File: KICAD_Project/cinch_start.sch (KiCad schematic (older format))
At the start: 27 parts, among them P101 CONN_1, P102 CONN_1, P103 CONN_1, P104 CONN_1, P105 CONN_1, P109 CONN_1, P110 CONN_1, P111 CONN_1, P112 CONN_1, P113 CONN_1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

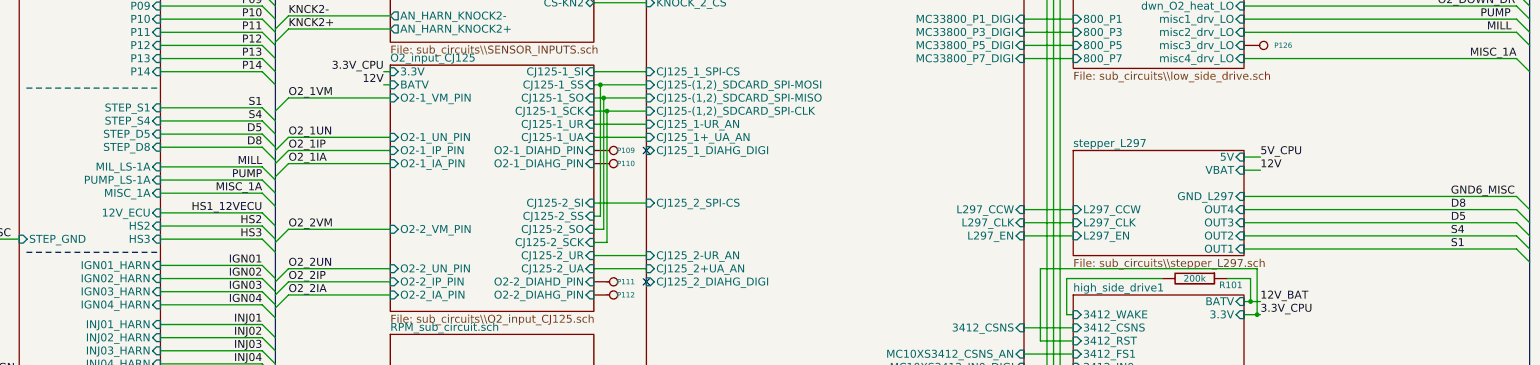
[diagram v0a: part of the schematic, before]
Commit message: changed stepper from L297 to A4988 from pololu
Signed-off-by: Jared Harvey <TortiseGIT@jaredharvey.com>
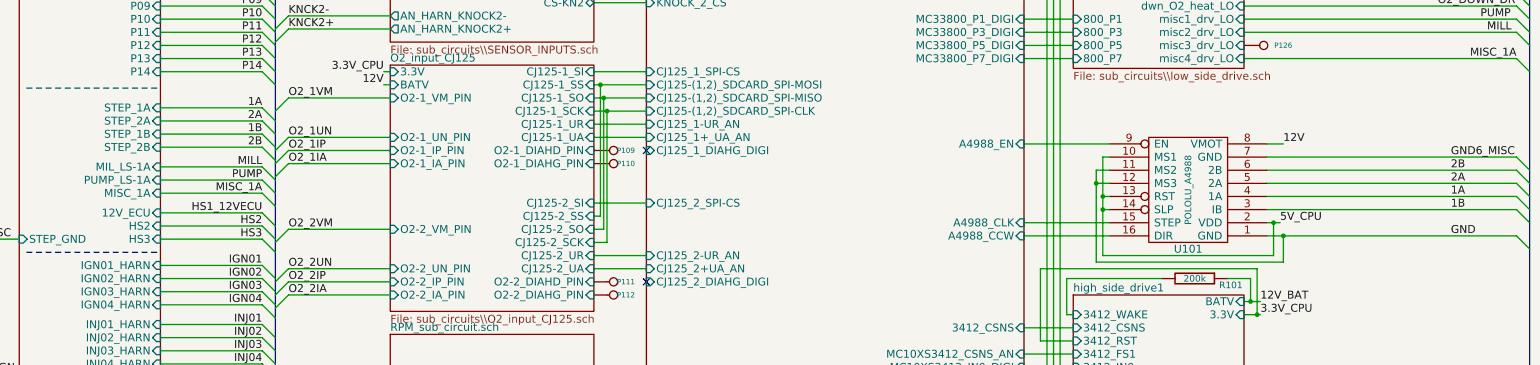
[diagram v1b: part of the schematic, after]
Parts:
- added U101: POLOLU_A4988, SWDIP8_.6W, symbol POLOLU_A4988
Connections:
- net 12V: now also U101.8 (VMOT)
- net 5V_CPU: now also U101.10 (MS1), U101.13 (RST), U101.14 (SLP), U101.2 (VDD)
- net GND: now also U101.1 (GND), U101.11 (MS2), U101.12 (MS3)
- net GND6_MISC: now also U101.7 (GND)
- new net 1A: U101.4 (1A)
- new net 1B: U101.3 (IB)
- new net 2A: U101.5 (2A)
- new net 2B: U101.6 (2B)
- new net CPU/A4988_CCW: U101.16 (DIR)
- new net CPU/A4988_CLK: U101.15 (STEP)
- new net CPU/A4988_EN: U101.9 (EN)
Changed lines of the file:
@@
-EESchema Schematic File Version 2  date 9/27/2011 11:45:21 AM
+EESchema Schematic File Version 2  date 10/2/2011 8:46:34 AM
 LIBS:power
 LIBS:device
@@
 $Descr C 22000 17000
 encoding utf-8
-Sheet 1 13
+Sheet 1 12
 Title "freeEMS PLUS from Cinch template "
-Date "27 sep 2011"
+Date "2 oct 2011"
 Rev "A-DRAFT5"
 Comp "diyefi.org/openecu.info"
@@
 Comment4 ""
 $EndDescr
+Connection ~ 13250 9525
+Connection ~ 14675 9925
+Wire Wire Line
+	14675 9925 14675 10125
+Wire Wire Line
+	14675 10125 13250 10125
+Wire Wire Line
+	13250 10125 13250 9425
+Wire Wire Line
+	16450 9325 14550 9325
+Wire Wire Line
+	12700 9925 13350 9925
+Wire Wire Line
+	12700 9225 13350 9225
+Connection ~ 13300 9625
+Wire Wire Line
+	13300 9625 13350 9625
+Wire Wire Line
+	16450 9925 14550 9925
+Connection ~ 14600 9825
+Wire Wire Line
+	14600 9825 14600 10075
+Wire Wire Line
+	14600 10075 13300 10075
+Wire Wire Line
+	13300 10075 13300 9325
 Wire Wire Line
 	12700 8575 13075 8575
@@
 Wire Wire Line
 	14375 8075 16450 8075
-Wire Wire Line
-	14375 9625 16450 9625
 Wire Wire Line
 	14375 5425 16450 5425
@@
 	14375 11525 16450 11525
 Wire Wire Line
-	14375 9925 16450 9925
-Wire Wire Line
-	14375 10025 16450 10025
-Wire Wire Line
-	14375 9825 16450 9825
-Wire Wire Line
-	14375 9725 16450 9725
+	16450 9625 14550 9625
+Wire Wire Line
+	16450 9725 14550 9725
+Wire Wire Line
+	16450 9525 14550 9525
+Wire Wire Line
+	16450 9425 14550 9425
 Wire Wire Line
 	14375 6500 16450 6500
@@
 	13125 12075 12700 12075
 Wire Wire Line
-	12700 9925 13075 9925
-Wire Wire Line
 	12700 11325 13075 11325
 Wire Wire Line
@@
 	13075 11425 12975 11425
 Connection ~ 12925 7975
-Wire Wire Line
-	12700 9725 13075 9725
 Wire Wire Line
 	12700 7775 13075 7775
@@
 	14375 7775 14500 7775
 Wire Wire Line
-	14375 9425 14500 9425
-Wire Wire Line
-	14500 9325 14375 9325
+	14550 9225 14675 9225
+Wire Wire Line
+	14550 9825 14650 9825
 Wire Wire Line
 	14500 7675 14375 7675
@@
 Wire Wire Line
 	12700 11225 13075 11225
-Wire Wire Line
-	12700 9825 13075 9825
 Wire Wire Line
 	13125 12175 12700 12175
@@
 Wire Wire Line
 	12700 8475 13075 8475
+Wire Wire Line
+	13300 9325 13350 9325
+Wire Wire Line
+	13300 9725 13350 9725
+Connection ~ 13300 9725
+Wire Wire Line
+	12700 9825 13350 9825
+Wire Wire Line
+	13250 9425 13350 9425
+Wire Wire Line
+	13250 9525 13350 9525
+Entry Wire Line
+	16450 9925 16550 10025
+Text Label 15950 9925 0    60   ~ 0
+GND
+$Comp
+L POLOLU_A4988 U101
+U 1 1 4E88435A
+P 13950 9575
+F 0 "U101" H 13950 10025 60  0000 C CNN
+F 1 "POLOLU_A4988" V 13950 9575 50  0000 C CNN
+F 2 "SWDIP8_.6W" H 13950 9575 60  0001 C CNN
+	1    13950 9575
+	-1   0    0    1
+$EndComp
 $Sheet
 S 9825 1750 2875 14500
@@
 F124 "RS232_2_TX" I R 12700 13525 60
 F125 "RS232_2_RX" I R 12700 13625 60
-F126 "L297_CLK" I R 12700 9825 60
-F127 "L297_CCW" I R 12700 9725 60
-F128 "L297_EN" I R 12700 9925 60
+F126 "A4988_CLK" I R 12700 9825 60
+F127 "A4988_CCW" I R 12700 9925 60
+F128 "A4988_EN" I R 12700 9225 60
 $EndSheet
 $Comp
@@
 F2 "232_TX" I R 6125 6950 60
 F3 "232_RX" I R 6125 7050 60
-F4 "STEP_S1" I R 6125 8950 60
-F5 "STEP_S4" I R 6125 9050 60
-F6 "STEP_D5" I R 6125 9150 60
-F7 "STEP_D8" I R 6125 9250 60
+F4 "STEP_1A" I R 6125 8950 60
+F5 "STEP_2A" I R 6125 9050 60
+F6 "STEP_1B" I R 6125 9150 60
+F7 "STEP_2B" I R 6125 9250 60
 F8 "FLEX_CAN_L" I R 6125 6750 60
 F9 "FLEX_CAN_H" I R 6125 6850 60
@@
 Text Label 15850 8175 0    60   ~ 0
 O2_DOWN_DR
-Text Label 15950 9625 0    60   ~ 0
+Text Label 15950 9325 0    60   ~ 0
 GND6_MISC
 Entry Wire Line
-	16450 9625 16550 9725
+	16450 9325 16550 9425
 Entry Wire Line
 	16450 5425 16550 5525
@@
 IGN12
 Text Label 6900 9250 2    60   ~ 0
-D8
+2B
 Text Label 6900 9150 2    60   ~ 0
-D5
+1B
 Text Label 6900 8950 2    60   ~ 0
-S1
+1A
 Text Label 6900 9050 2    60   ~ 0
-S4
+2A
 Text Label 6900 9850 2    60   ~ 0
 HS2
@@
 HS2
 Entry Wire Line
-	16450 9925 16550 10025
-Text Label 15950 9925 0    60   ~ 0
-S4
-Text Label 15950 10025 0    60   ~ 0
-S1
-Entry Wire Line
-	16450 10025 16550 10125
-Entry Wire Line
-	16450 9825 16550 9925
-Text Label 15950 9825 0    60   ~ 0
-D5
+	16450 9625 16550 9725
+Text Label 15950 9625 0    60   ~ 0
+1A
 Text Label 15950 9725 0    60   ~ 0
-D8
+1B
 Entry Wire Line
 	16450 9725 16550 9825
+Entry Wire Line
+	16450 9525 16550 9625
+Text Label 15950 9525 0    60   ~ 0
+2A
+Text Label 15950 9425 0    60   ~ 0
+2B
+Entry Wire Line
+	16450 9425 16550 9525
 Entry Wire Line
 	16450 6500 16550 6600
@@
 Text Label 14500 7675 0    60   ~ 0
 3.3V_CPU
-Text Label 14500 9325 0    60   ~ 0
+Text Label 14650 9825 0    60   ~ 0
 5V_CPU
-Text Label 14500 9425 0    60   ~ 0
+Text Label 14675 9225 0    60   ~ 0
 12V
 Text Label 14500 7775 0    60   ~ 0
@@
 12V
 $Sheet
-S 13075 9275 1300 800
-U 4C0F6CBF
-F0 "stepper_L297" 60
-F1 "sub_circuits\\stepper_L297.sch" 60
-F2 "5V" I R 14375 9325 60
-F3 "VBAT" I R 14375 9425 60
-F4 "OUT4" I R 14375 9725 60
-F5 "GND_L297" I R 14375 9625 60
-F6 "OUT3" I R 14375 9825 60
-F7 "OUT2" I R 14375 9925 60
-F8 "OUT1" I R 14375 10025 60
-F9 "L297_CCW" I L 13075 9725 60
-F10 "L297_CLK" I L 13075 9825 60
-F11 "L297_EN" I L 13075 9925 60
-$EndSheet
-$Sheet
 S 13075 10375 1300 1325

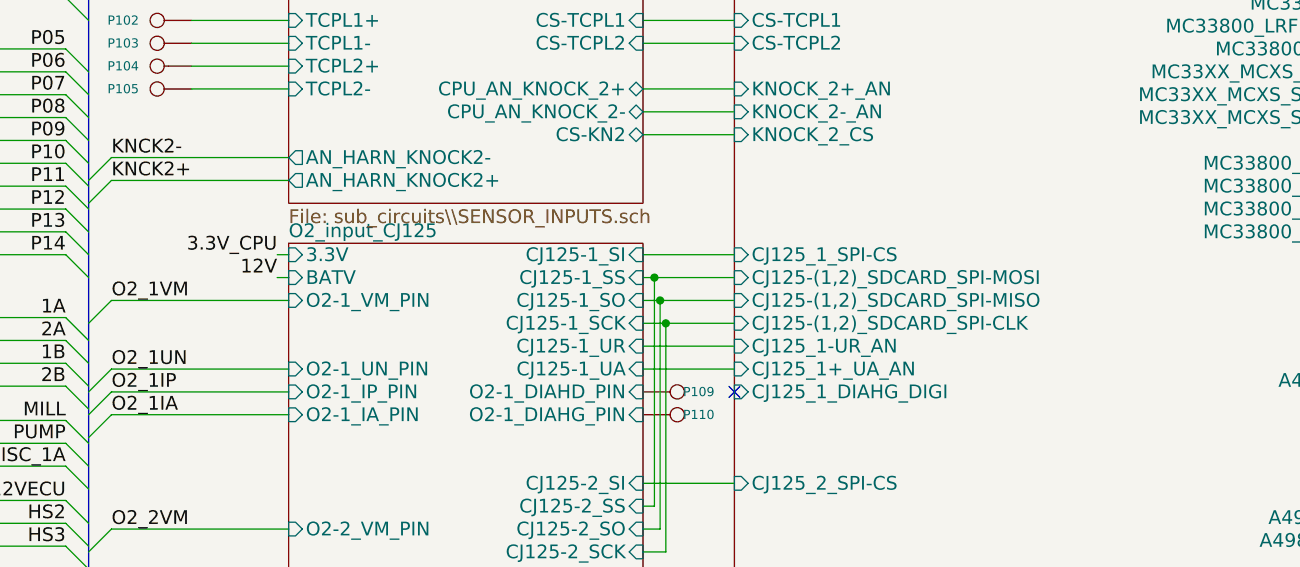
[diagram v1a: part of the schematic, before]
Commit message: Added some simulations for the AN protect lines
Signed-off-by: Jared Harvey <TortiseGIT@jaredharvey.com>
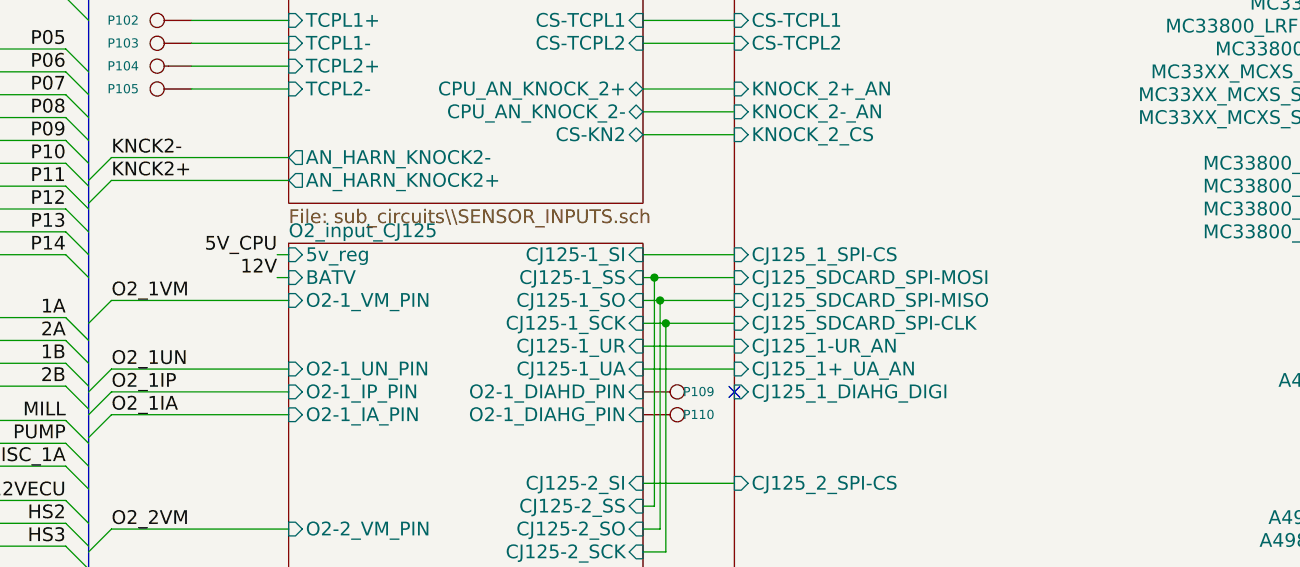
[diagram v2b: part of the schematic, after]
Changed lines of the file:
@@
-EESchema Schematic File Version 2  date 10/2/2011 8:46:34 AM
+EESchema Schematic File Version 2  date 10/4/2011 8:27:03 PM
 LIBS:power
 LIBS:device
@@
 Sheet 1 12
 Title "freeEMS PLUS from Cinch template "
-Date "2 oct 2011"
+Date "5 oct 2011"
 Rev "A-DRAFT5"
 Comp "diyefi.org/openecu.info"
@@
 F26 "MC33XX_MCXS_SPI-MISO" I R 12700 8075 60
 F27 "MC33XX_MCXS_SPI-CLK" I R 12700 7875 60
-F28 "CJ125-(1,2)_SDCARD_SPI-MOSI" I L 9825 8775 60
-F29 "CJ125-(1,2)_SDCARD_SPI-MISO" I L 9825 8875 60
-F30 "CJ125-(1,2)_SDCARD_SPI-CLK" I L 9825 8975 60
 F31 "CJ125_2_SPI-CS" I L 9825 9675 60
 F32 "CJ125_1_SPI-CS" I L 9825 8675 60
@@
 F127 "A4988_CCW" I R 12700 9925 60
 F128 "A4988_EN" I R 12700 9225 60
+F129 "CJ125_SDCARD_SPI-MOSI" I L 9825 8775 60
+F130 "CJ125_SDCARD_SPI-MISO" I L 9825 8875 60
+F131 "CJ125_SDCARD_SPI-CLK" I L 9825 8975 60
 $EndSheet
 $Comp
@@
 12V_BAT
 Text Label 7825 8675 2    60   ~ 0
-3.3V_CPU
+5V_CPU
 Text Label 9775 2200 2    60   ~ 0
 ENABLE_PWR
@@
 F0 "O2_input_CJ125" 60
 F1 "sub_circuits\\O2_input_CJ125.sch" 60
-F2 "3.3V" I L 7875 8675 60
 F3 "BATV" I L 7875 8775 60
 F4 "CJ125-1_UA" I R 9425 9175 60
@@
 F26 "CJ125-2_UR" I R 9425 10075 60
 F27 "CJ125-2_UA" I R 9425 10175 60
+F28 "5v_reg" I L 7875 8675 60
 $EndSheet
 $Sheet

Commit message: Made more progress on the AN protects and LS drive 33800
Signed-off-by: Jared Harvey <TortiseGIT@jaredharvey.com>
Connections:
- net low_side_drive1/misc3_drv_LO renamed low_side_drive1/misc4_drv_LO
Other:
- moved on the sheet: P126
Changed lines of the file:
@@
-EESchema Schematic File Version 2  date 10/14/2011 5:26:21 AM
+EESchema Schematic File Version 2  date 10/16/2011 7:32:21 AM
 LIBS:power
 LIBS:device
@@
 Sheet 1 12
 Title "Open5xxxECU (o5e), an ECU that is no longer affiliated with freeEMS."
-Date "14 oct 2011"
+Date "16 oct 2011"
 Rev "A-DRAFT5"
 Comp "http://open5xxxecu.org/"
@@
 Comment4 ""
 $EndDescr
+$Sheet
+S 13075 7525 1300 1125
+U 4C0E2D2F
+F0 "low_side_drive1" 60
+F1 "sub_circuits\\low_side_drive.sch" 60
+F2 "BATV" I R 14375 7575 60
+F3 "EN0" I L 13075 7575 60
+F4 "800_LRFDBK" I L 13075 7675 60
+F5 "800_CS" I L 13075 7775 60
+F6 "800_SCLK" I L 13075 7875 60
+F7 "800_SI" I L 13075 7975 60
+F8 "3.3V" I R 14375 7675 60
+F9 "12v" I R 14375 7775 60
+F10 "up_O2_heat_LO" I R 14375 8075 60
+F11 "dwn_O2_heat_LO" I R 14375 8175 60
+F12 "misc2_drv_LO" I R 14375 8375 60
+F13 "misc3_drv_LO" I R 14375 8475 60
+F14 "misc4_drv_LO" I R 14375 8575 60
+F15 "misc1_drv_LO" I R 14375 8275 60
+F16 "800_SO" I L 13075 8075 60
+F17 "GND_MC33800" I R 14375 7975 60
+F18 "800_P7" I L 13075 8575 60
+F19 "800_P3" I L 13075 8375 60
+F20 "800_P5" I L 13075 8475 60
+F21 "800_P1" I L 13075 8275 60
+$EndSheet
 Connection ~ 13250 9525
 Connection ~ 14675 9925
@@
 	12925 7975 12925 11950
 Wire Wire Line
-	14375 8575 16450 8575
+	14375 8475 16450 8475
 Wire Wire Line
 	14375 8375 16450 8375
@@
 L CONN_1 P126
 U 1 1 4E4F9546
-P 14525 8475
-F 0 "P126" H 14605 8475 40  0000 L CNN
-F 1 "CONN_1" H 14525 8530 30  0001 C CNN
-F 2 "PINTST" H 14525 8475 60  0001 C CNN
-	1    14525 8475
+P 14525 8575
+F 0 "P126" H 14605 8575 40  0000 L CNN
+F 1 "CONN_1" H 14525 8630 30  0001 C CNN
+F 2 "PINTST" H 14525 8575 60  0001 C CNN
+	1    14525 8575
 	1    0    0    -1
 $EndComp
@@
 HS1_12VECU
 Entry Wire Line
-	16450 8575 16550 8675
-Text Label 16450 8575 2    60   ~ 0
+	16450 8475 16550 8575
+Text Label 16450 8475 2    60   ~ 0
 MISC_1A
 Text Label 16225 8375 0    60   ~ 0
@@
 $EndSheet
 $Sheet
-S 13075 7525 1300 1125
-U 4C0E2D2F
-F0 "low_side_drive1" 60
-F1 "sub_circuits\\low_side_drive.sch" 60
-F2 "BATV" I R 14375 7575 60
-F3 "EN0" I L 13075 7575 60
-F4 "800_LRFDBK" I L 13075 7675 60
-F5 "800_CS" I L 13075 7775 60
-F6 "800_SCLK" I L 13075 7875 60
-F7 "800_SI" I L 13075 7975 60
-F8 "3.3V" I R 14375 7675 60
-F9 "12v" I R 14375 7775 60
-F10 "up_O2_heat_LO" I R 14375 8075 60
-F11 "dwn_O2_heat_LO" I R 14375 8175 60
-F12 "misc2_drv_LO" I R 14375 8375 60
-F13 "misc3_drv_LO" I R 14375 8475 60
-F14 "misc4_drv_LO" I R 14375 8575 60
-F15 "misc1_drv_LO" I R 14375 8275 60
-F16 "800_SO" I L 13075 8075 60
-F17 "GND_MC33800" I R 14375 7975 60
-F18 "800_P7" I L 13075 8575 60
-F19 "800_P3" I L 13075 8375 60
-F20 "800_P5" I L 13075 8475 60
-F21 "800_P1" I L 13075 8275 60
-$EndSheet
-$Sheet
